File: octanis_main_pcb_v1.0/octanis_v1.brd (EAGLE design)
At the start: 81 x 50 mm, 107 parts, among them IC1 BNO055A, IC2 BME280, Q1 32.768kHz, Q2 32.768kHz, U1 TPS61232, U10 INA210, U100 RN2483, U11 DRV8836DSSR, U12 DRV8836DSSR, U2 MSP432, U3 MAX6001SOT-23, U4 DRV8836DSSR, U5 DRV8836DSSR, U6 SST25VF064C, U7 INA210, U8 INA210, U9 INA210

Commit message: started v1.0 mainboard
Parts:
- removed 5V: 5V-ok, adafruit:CHIPLED_0603
- removed C10: 10nF, rcl:C0603
- removed JP1: (no value), pinhead-2:2X05
- removed LED33_J: (no value), jumper:SJ
- removed U1: TPS61232, texasinstruments:S-PVSON-N10
- added BAT: BAT-ok, adafruit:CHIPLED_0603
- added C36, C37: 470n, rcl:C0603
- added IC3: TPS61201, texas:S-PDSO-N10
- added JP4: (no value), pinhead-2:2X06SMD
- added TP1, TP2: TPTP06R, testpad:TP06R
- C1, C7, C8: value 22uF -> 10u; device rcl:C0603 -> rcl:C0805K
- C9: value 3 x 22uF -> 100n
- JP2: device pinhead-2:2X05SMD -> pinhead-2:2X04
- L1: value 1uH -> LPS3015; device Coilcraft:XFL4020 -> inductor-coilcraft:LPS3015
- moved JP2 19.5 mm to (5.03, 6.10)
- moved 3V 13.2 mm to (13.1, 14.5), turned to 270 degrees
- moved R1 9.87 mm to (11.3, 3.05)
- moved LED5_J 8.54 mm to (13.5, 10.9)
- moved R6 8.20 mm to (16.0, 12.1), flipped to the bottom, turned to 90 degrees
- moved R8 5.31 mm to (17.6, 12.1), flipped to the bottom, turned to 90 degrees
- moved L1 5.17 mm to (12.2, 10.6)
- moved U$1 4.89 mm to (21.3, 18.4)
- moved C8 4.17 mm to (21.3, 6.35), turned to 270 degrees
- moved C1 3.77 mm to (10.5, 6.35)
- moved C9 3.69 mm to (16.8, 6.35), turned to 270 degrees
- moved C7 3.57 mm to (18.7, 6.35), turned to 270 degrees
- moved V_MOT1 2.54 mm to (58.9, 4.78)
- moved R7 2.22 mm to (14.6, 3.05), turned to 180 degrees
- moved C26 0.20 mm to (66.1, 15.6)
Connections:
- removed net IND: L1.P$2, U1.1, U1.2
- removed net N$14: LED5_J.2, R6.1
- removed net P7.5: DIGITAL_IO2.10, U2.27
- removed net P7.6: DIGITAL_IO2.9, U2.28
- new net L: IC3.3, L1.2
- new net N$20: TP2.TP, U5.11
- new net N$22: TP1.TP, U4.11
- new net P8.0: DIGITAL_IO2.10, U2.30
- new net P8.1: DIGITAL_IO2.9, U2.31
- net +3V3: now also C7.1, C8.1, IC3.2, JP4.10, JP4.3, JP4.9; no longer JP2.10, JP2.3, JP2.9
- net +5V: now also JP2.7, JP2.8; no longer 5V.A, C7.1, C8.1, C9.1, JP1.10, JP1.9, R7.2, U1.3, U1.4, U1.7
- net 3V3_MODULE2: now also BAT.A, IC3.5, IC3.6, IC3.8, JP2.3, JP2.4, L1.1; no longer JP1.5, JP1.6, L1.P$1, U1.10
- net 5VEN: no longer R1.1, U1.9
- net EXT_LIGHTNING_INT: now also JP4.2; no longer JP2.2
- net EXT_UV_EN: now also JP4.1; no longer JP2.1
- net GND: now also C36.2, C37.2, IC3.4, IC3.9, IC3.PP, IC3.PP@1, IC3.PP@2, JP2.1, JP2.2, JP2.5, JP2.6, JP4.11, JP4.12, JP4.4, R7.1; no longer C10.2, JP1.1, JP1.2, JP1.3, JP1.4, JP1.7, JP1.8, JP2.4, LED33_J.1, U1.EXPAD, U1.GND1, U1.GND2, U1.GND3, U1.GND4, U1.GND5
- net M5678SLEEP: now also C36.1, C37.1; no longer U4.11, U5.11
- net M5IN1: now also U2.27; no longer U2.29
- net M5IN2: now also U2.28; no longer U2.30
- net M6IN1: now also U2.29; no longer U2.32
- net M6IN2: now also U2.32; no longer U2.31
- net N$2: now also C9.1, IC3.1; no longer R7.1, U1.5
- net N$26: now also LED5_J.2, R6.1; no longer LED33_J.2
- net N$42: now also IC3.7, R1.1, R7.2; no longer C10.1, U1.6
- net N$44: now also BAT.C; no longer 5V.C
- net SCL: now also JP4.5, JP4.7; no longer JP2.5, JP2.7
- net SDA: now also JP4.6, JP4.8; no longer JP2.6, JP2.8
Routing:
- net 3V3_MODULE2: track 105.4 -> 145.0 mm, vias 1 -> 3
- net 5VEN: track 35.5 -> 0.00 mm
- net P8.1: track 0.00 -> 19.1 mm, vias 0 -> 2
- net P8.0: track 0.00 -> 16.0 mm, vias 0 -> 2
- net P7.6: track 14.5 -> 0.00 mm
- net GND: track 113.3 -> 126.6 mm, vias 62 -> 66
- net +3V3: track 301.5 -> 289.2 mm, vias 13 -> 11
- net P7.5: track 11.3 -> 0.00 mm
- net +5V: track 93.9 -> 83.9 mm, vias 1 -> 0
- net M5678SLEEP: track 36.9 -> 28.7 mm
- net N$4: track 1.80 -> 5.03 mm, vias 0 -> 1
- net N$2: track 4.65 -> 2.43 mm, vias 2 -> 0
- net V_MOTOR2: track 23.2 -> 25.2 mm
- net N$42: track 1.45 -> 3.35 mm
- net N$14: track 1.86 -> 0.00 mm, vias 1 -> 0
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- added copper zone on layer 1, net L
- removed copper zone on layer 1, net +5V
- removed copper zone on layer 1, net IND

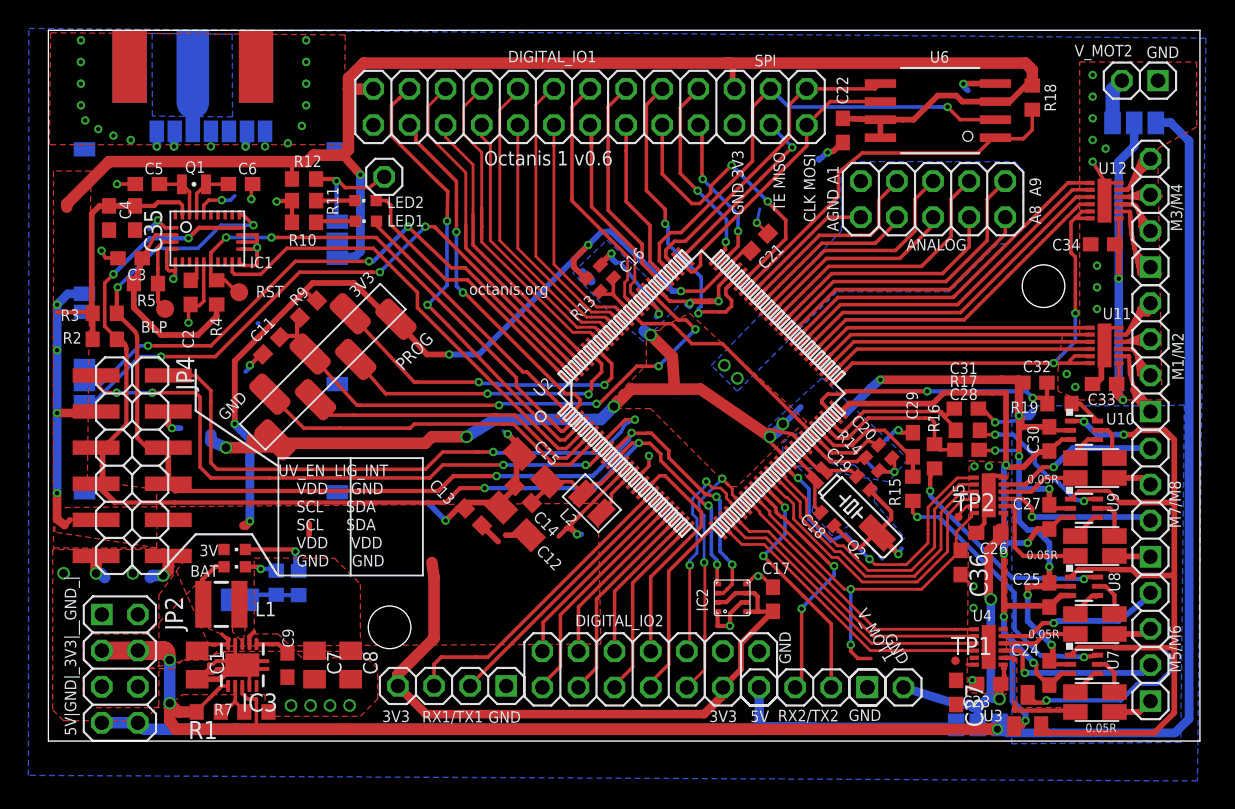
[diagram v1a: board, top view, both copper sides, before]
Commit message: added 5V on-off switch and battery boost converter to mainboard
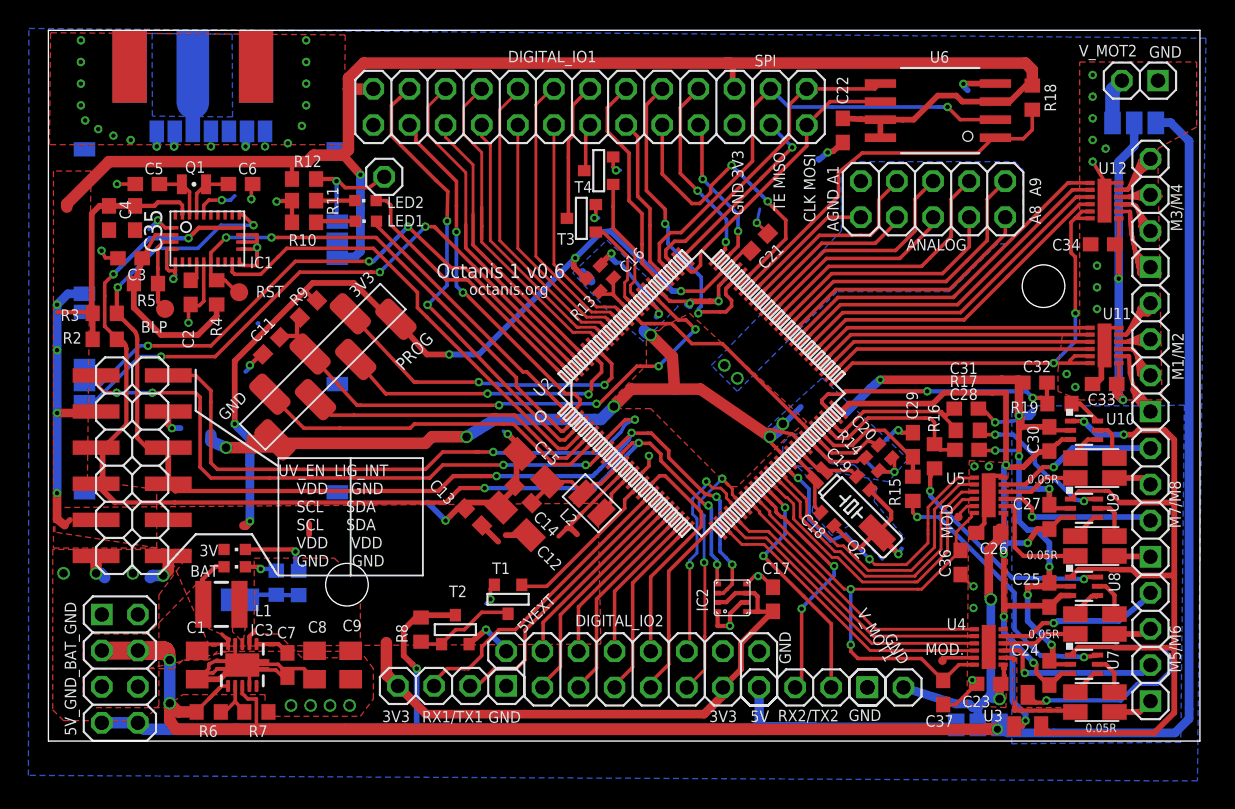
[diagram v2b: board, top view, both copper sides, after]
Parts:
- removed R1: 1M, rcl:R0603
- removed TP1: TPTP06R, testpad:TP06R
- added 5VEXT: (no value), Headerlibrary:1X01
- added MOD.: TPTP06R, testpad:TP06R
- added R101: 2k, rcl:R0603
- added R102: 1k, rcl:R0603
- added T1, T2, T3, T4: (no value), zetex:SOT-23
- C7: value 10u -> 100n; device rcl:C0805K -> rcl:C0603
- C9: value 100n -> 10u; device rcl:C0603 -> rcl:C0805K
- R6: value 2k -> 1M
- R8: value 1k -> 1M
- moved R6 10.3 mm to (11.3, 3.05), flipped to the top, turned to 180 degrees
- moved R8 9.21 mm to (26.2, 8.84), flipped to the top
- moved C9 4.44 mm to (21.3, 6.35)
- moved C8 2.54 mm to (18.7, 6.35)
- moved C7 1.90 mm to (16.8, 6.35)
- moved C37 0.91 mm to (62.9, 4.42)
- renumbered TP2 to MOD
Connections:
- removed net 5VEN: U2.16
- new net 5V_EN: T1.3, U2.16
- new net N$14: R8.1, T1.1, T2.3
- new net N$46: DIGITAL_IO1.9, T3.1
- new net N$47: 5VEXT.1, T2.2
- new net N$55: DIGITAL_IO1.10, T4.1
- net +3V3: now also C9.1; no longer C7.1
- net +5V: now also R8.2, T2.1
- net 3V3_MODULE2: now also R6.2; no longer R1.2
- net GND: now also T1.2, T3.2, T4.2
- net N$2: now also C7.1; no longer C9.1
- net N$22: now also MOD..TP; no longer TP1.TP
- net N$26: now also R101.1, R102.1; no longer R6.1, R8.1
- net N$4: now also R102.2; no longer R8.2
- net N$42: now also R6.1; no longer R1.1
- net N$44: now also R101.2; no longer R6.2
- net PJ.2: now also T4.3; no longer DIGITAL_IO1.10
- net PJ.3: now also T3.3; no longer DIGITAL_IO1.9
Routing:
- net GND: track 126.6 -> 143.3 mm, vias 66 -> 69
- net 5V_EN: track 0.00 -> 11.7 mm
- net PJ.3: track 17.9 -> 6.37 mm
- net +5V: track 83.9 -> 95.3 mm, vias 0 -> 1
- net N$46: track 0.00 -> 9.82 mm
- net +3V3: track 289.2 -> 281.2 mm, vias 11 -> 10
- net M5678SLEEP: track 28.7 -> 36.6 mm
- net N$14: track 0.00 -> 7.13 mm
- net PJ.2: track 15.2 -> 9.29 mm
- net N$47: track 0.00 -> 3.65 mm, vias 0 -> 1
- net N$55: track 0.00 -> 3.38 mm
- net N$22: track 0.00 -> 2.44 mm
- net TX1: track 18.5 -> 19.7 mm
- net 3V3_MODULE2: track 145.0 -> 145.7 mm
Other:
- board text added: "5V_GND_BAT_GND"
- board text removed: "5V|GND|_3V3|__GND_|"

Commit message: silkscreen artwork, lightning input interrupt
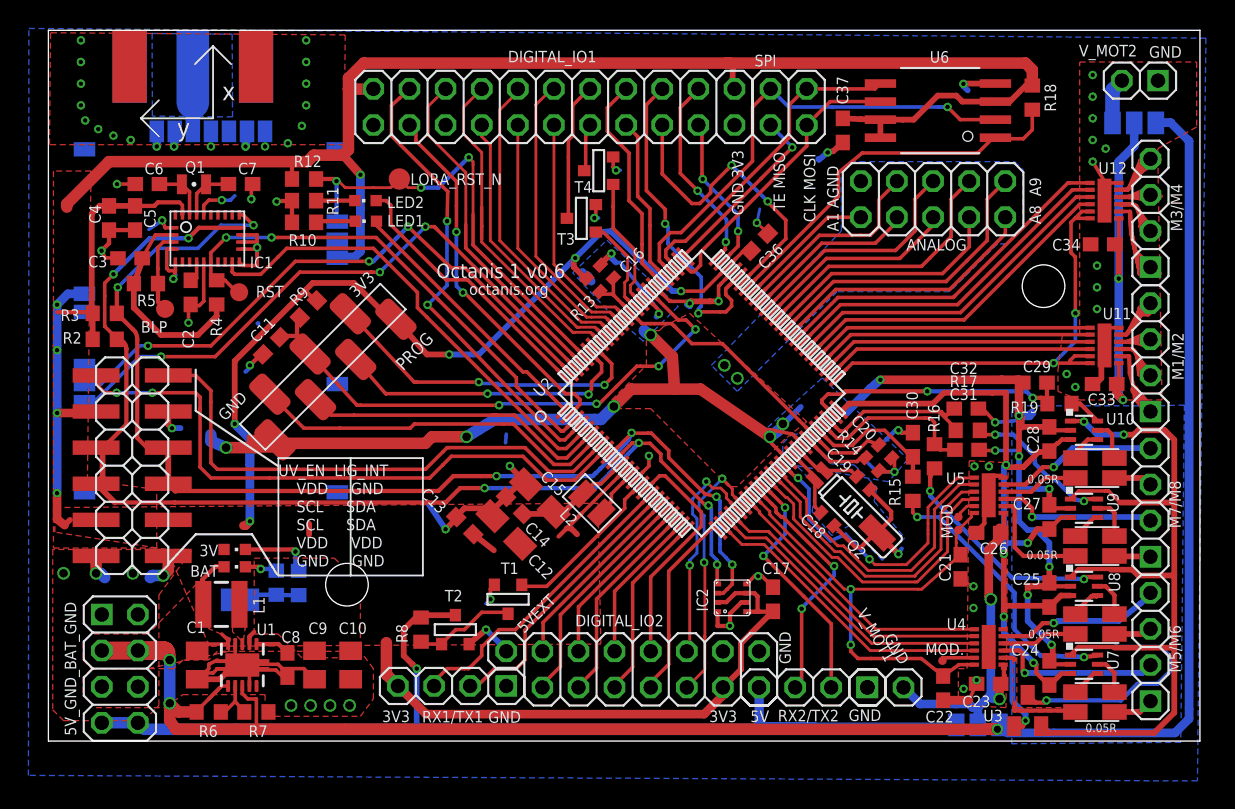
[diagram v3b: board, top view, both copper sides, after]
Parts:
- removed C35: 120n, rcl:C0603
- added C10: 10u, rcl:C0805K
- added U$3: BNO055_COORDINATES, Octanis1:BNO055_COORDINATES
- added VCCMOT: TPTP06R, testpad:TP06R
- C21, C22: value 100n -> 470n
- C28: value 470n -> 10n
- C30: value 10n -> 470n
- C36, C37: value 470n -> 100n
- C5: value 12p -> 120n
- C7: value 100n -> 12p
- C8: value 10u -> 100n; device rcl:C0805K -> rcl:C0603
- LORA_RST_N: value (none) -> PTR1TP15R; device Headerlibrary:1X01 -> testpad:TP15R
- moved C37 40.2 mm to (55.9, 44.0)
- moved C22 39.9 mm to (62.9, 4.72)
- moved C7 34.0 mm to (13.5, 40.2), turned to 0 degrees
- moved C21 26.9 mm to (64.2, 13.3), turned to 270 degrees
- moved C36 26.6 mm to (50.0, 36.1), turned to 225 degrees
- moved C29 9.63 mm to (69.4, 26.2), turned to 0 degrees
- moved C30 9.61 mm to (60.8, 21.8)
- moved C6 6.55 mm to (6.96, 40.2), turned to 180 degrees
- moved C28 5.84 mm to (70.4, 22.3), turned to 270 degrees
- moved C32 5.16 mm to (64.6, 24.4), turned to 180 degrees
- moved C31 2.90 mm to (64.6, 21.5)
- moved C9 2.54 mm to (18.7, 6.35)
- moved C5 2.54 mm to (6.10, 37.8), turned to 270 degrees
- moved C15 2.18 mm to (34.6, 18.1)
- moved C8 1.90 mm to (16.8, 6.35)
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- renumbered IC3 to U1
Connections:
- removed net P9.4: DIGITAL_IO1.18, U2.96
- net +3V3: now also C10.1, C36.2, C37.1, C5.1; no longer C21.2, C22.1, C35.1, C8.1
- net A20: now also C29.2; no longer C32.2
- net A21: now also C32.2; no longer C31.2
- net A22: now also C31.2; no longer C28.2
- net A23: now also C30.2; no longer C29.2
- net CURR_SENSE_EN: now also C28.2; no longer C30.2
- net GND: now also C10.2, C21.2, C36.1, DIGITAL_IO1.18; no longer C21.1, C35.2, C36.2
- net LORA_RST_N: now also LORA_RST_N.TP, U2.96; no longer LORA_RST_N.1
- net M5678SLEEP: now also C21.1, C22.1, VCCMOT.TP; no longer C36.1, C37.1
- net N$19: now also C6.1; no longer C5.1
- net N$2: now also C8.1; no longer C7.1
- net N$73: now also C7.1; no longer C6.1
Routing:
- net LORA_RST_N: track 8.22 -> 32.7 mm, vias 1 -> 3
- net P9.4: track 20.4 -> 0.00 mm
- net EXT_LIGHTNING_INT: track 43.8 -> 38.7 mm, vias 2 -> 0
- net EXT_UV_EN: track 42.6 -> 43.9 mm, vias 4 -> 2
- net +3V3: track 281.2 -> 280.4 mm
- net GND: track 143.3 -> 143.0 mm, vias 69 -> 70
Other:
- board text added: "A1 AGND"
- board text removed: "AGND A1"

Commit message: octanis 1.0 finished
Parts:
- moved T1 1.83 mm to (30.5, 11.0)
- moved LORA_RST_N 0.15 mm to (24.7, 40.7)
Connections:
- net 5V_EN: now also U2.8; no longer U2.16
- net EXT_LIGHTNING_INT: now also U2.16; no longer U2.8
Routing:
- net 5V_EN: track 11.7 -> 26.9 mm, vias 0 -> 2
- net EXT_LIGHTNING_INT: track 38.7 -> 50.9 mm, vias 0 -> 2
- net +3V3: track 280.4 -> 284.1 mm
- net GND: track 143.0 -> 141.0 mm
- net N$14: track 7.13 -> 5.35 mm
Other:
- board size 81 x 50 mm -> 82 x 50 mm
- board text added: "Octanis 1 v1.0"
- board text added: "mainboard"
- board text removed: "Octanis 1 v0.6"

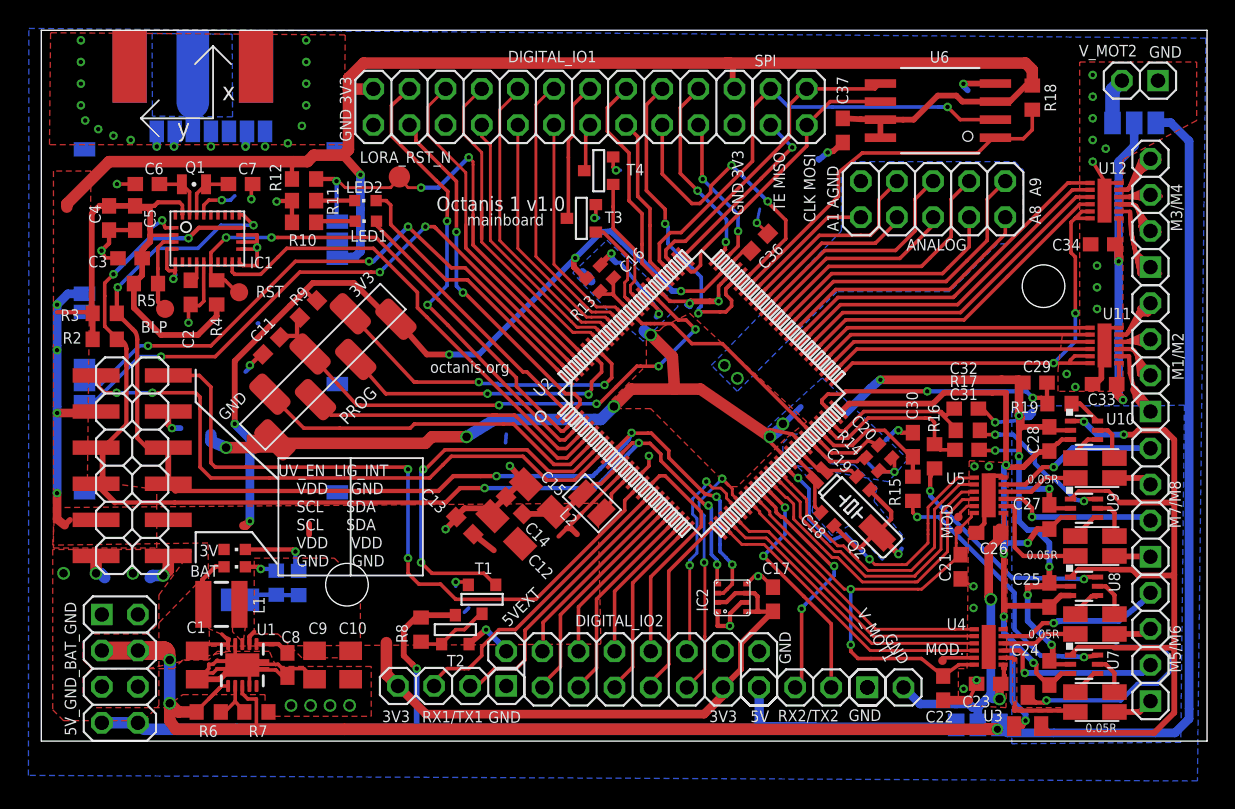
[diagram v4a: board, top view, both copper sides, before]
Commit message: weather strip v3. revised mainboard v1
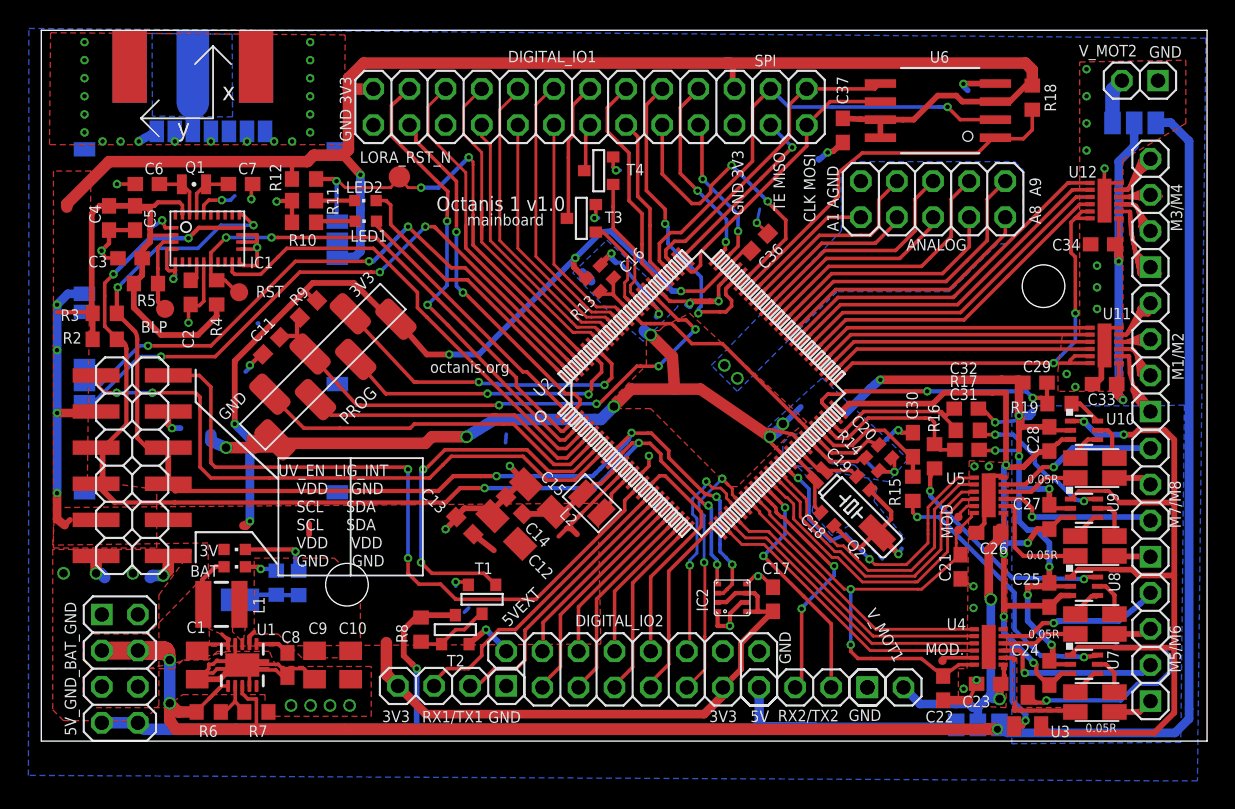
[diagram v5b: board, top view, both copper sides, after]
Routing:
- net GND: track 141.0 -> 139.9 mm
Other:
- board text added: "BAT V_mot 5V"
- board text added: "BAT V_mot V_ext"
- board text removed: "3V3 V_mot 5V"
- board text removed: "3V3 V_mot V_ext"
